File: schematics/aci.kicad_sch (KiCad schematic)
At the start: 10 parts, among them J1 From Tape, U11 LM339, U12 74HC10, U13 74HC02

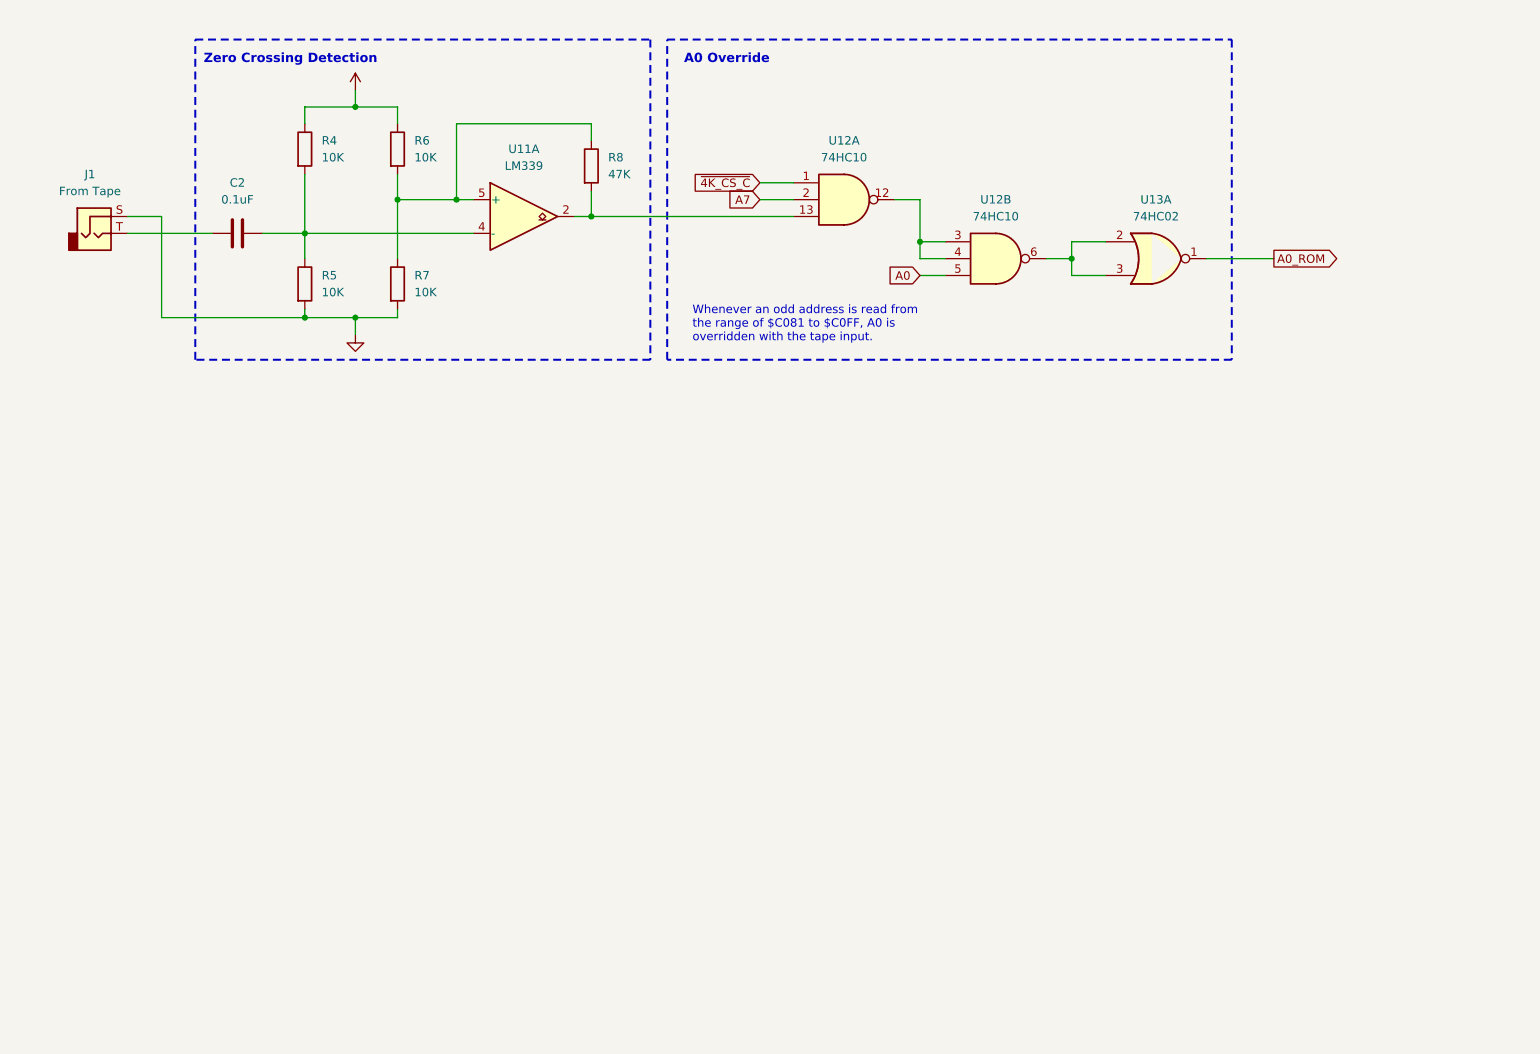
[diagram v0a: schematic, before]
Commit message: schematics updates
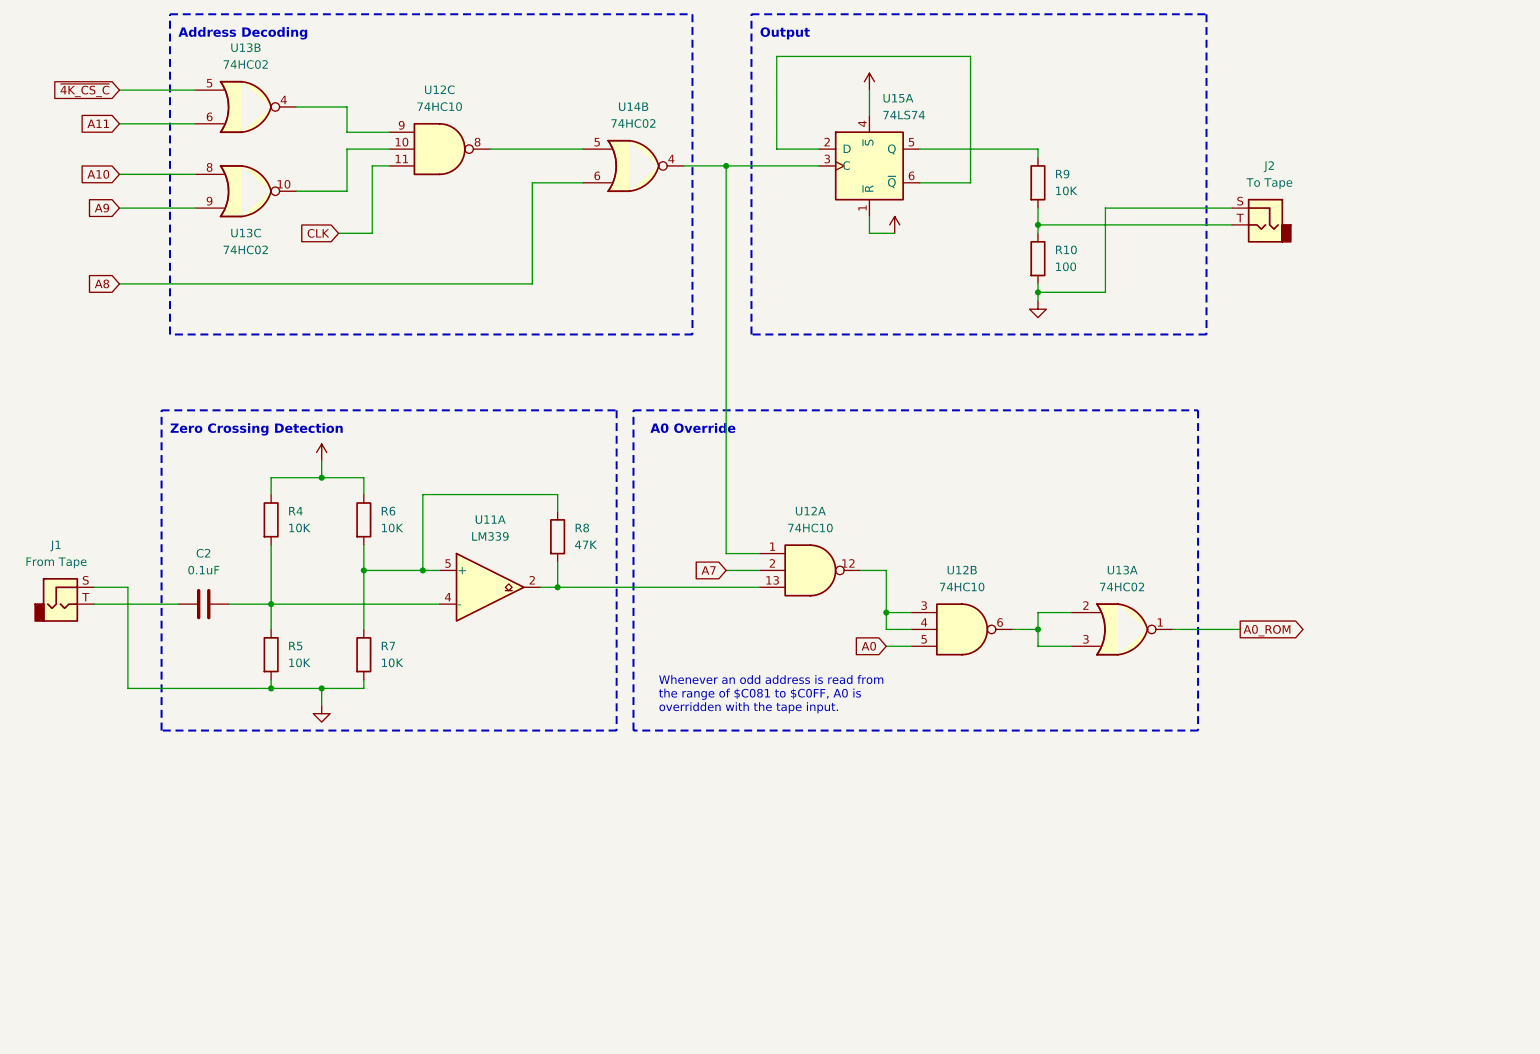
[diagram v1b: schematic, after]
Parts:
- added J2: To Tape, symbol Connector_Audio:AudioJack2
- added R10: 100, symbol Device:R
- added R9: 10K, symbol Device:R
- added unit 3 of U12
- added unit 3 of U13
- added unit 2 of U13
- added U14: 74HC02, symbol 74xx:74HC02
- added U15: 74LS74, symbol 74xx:74LS74
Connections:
- net GND: now also J2.S, R10.2
- net VCC: now also U15.1 (~{R}), U15.4 (~{S})
- net ~{4K_CS_C}: now also U13.5; no longer U12.1
- new net: J2.T, R10.1, R9.2
- new net: U12.10, U13.10
- new net: U12.8, U14.5
- new net: U12.9, U13.4
- new net: R9.1, U15.5 (Q)
- new net: U15.2 (D), U15.6 (~{Q})
- new net: U12.1, U14.4, U15.3 (C)
- new net A10: U13.8
- new net A11: U13.6
- new net A8: U14.6
- new net A9: U13.9
- new net CLK: U12.11
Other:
- note added: "Address Decoding"
- note added: "Output"
- moved on the sheet: C2, J1, R4, R5, R6, R7, R8, U11A, U12A, U12B, U13A

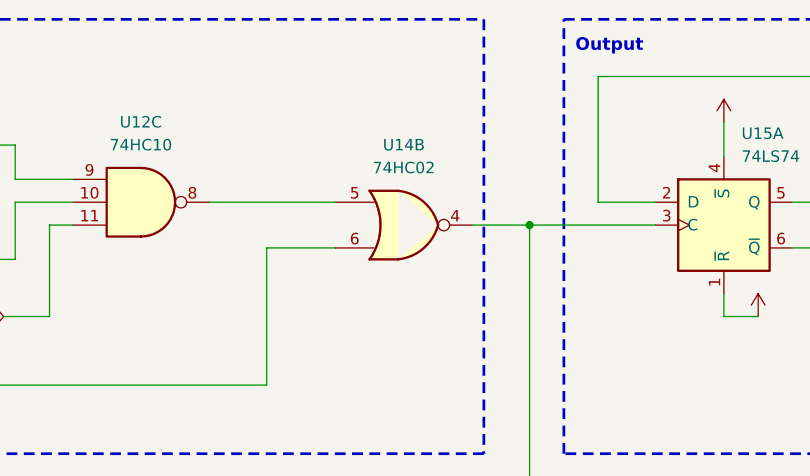
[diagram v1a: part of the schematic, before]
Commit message: minor correction to schematics
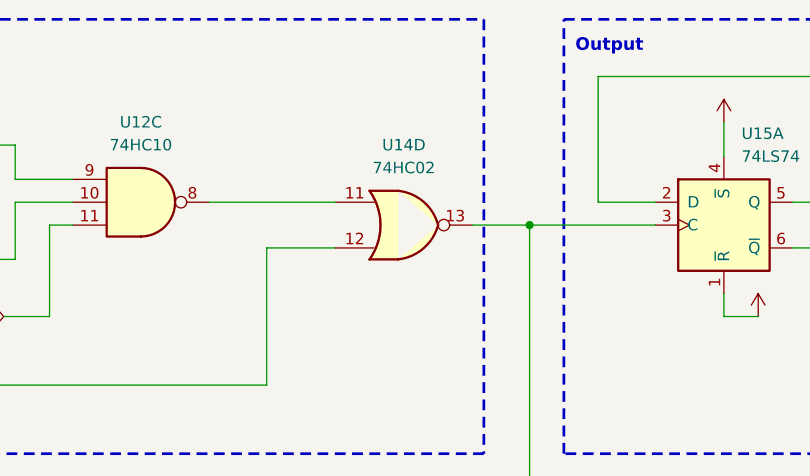
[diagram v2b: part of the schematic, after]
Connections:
- net A8: now also U14.12; no longer U14.6
- net at U12.8: now also U14.11; no longer U14.5
- net at U12.1, U15.3 (C): now also U14.13; no longer U14.4
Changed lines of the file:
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@@
     )
   )
-  (symbol (lib_id "74xx:74HC02") (at 127 44.45 0) (unit 2)
+  (symbol (lib_id "74xx:74HC02") (at 127 44.45 0) (unit 4)
     (in_bom yes) (on_board yes) (dnp no) (fields_autoplaced)
     (property "Reference" "U14" (at 127 35.56 0)
@@
       (project "apple-1"
         (path "/49da186c-18fb-4ced-8737-786ea50767d0/08d01d12-1e76-4903-ba4b-59c171f11e17"
-          (reference "U14") (unit 2)
+          (reference "U14") (unit 4)
         )
       )

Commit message: updates to schematics and 6502 source for ACI
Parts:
- R4, R5: value 10K -> 680K
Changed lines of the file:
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@@
       (effects (font (size 1.27 1.27)) (justify left))
     )
-    (property "Value" "10K" (at 74.93 99.06 0)
+    (property "Value" "680K" (at 74.93 99.06 0)
       (effects (font (size 1.27 1.27)) (justify left))
     )
@@
       (effects (font (size 1.27 1.27)) (justify left))
     )
-    (property "Value" "10K" (at 74.93 119.38 0)
-      (effects (font (size 1.27 1.27)) (justify left))
-    )
+    (property "Value" "680K" (at 74.93 119.38 0)
+      (effects (font (size 1.27 1.27)) (justify left))
+    )

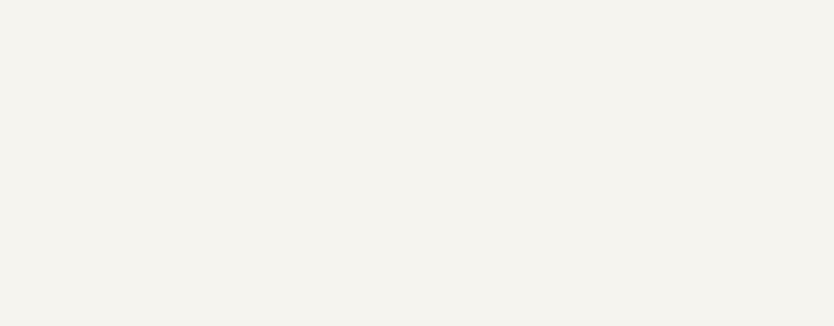
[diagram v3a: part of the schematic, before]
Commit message: added UART to design
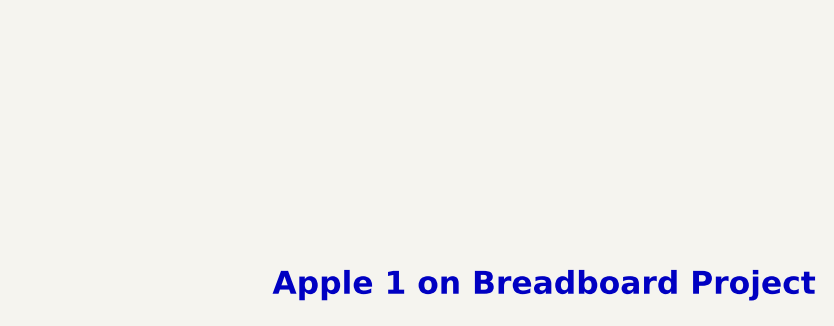
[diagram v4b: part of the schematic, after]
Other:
- note added: "Apple 1 on Breadboard Project"
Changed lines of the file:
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@@
     (effects (font (size 1.4 1.4) (thickness 0.28) bold) (justify left bottom))
+  )
+  (text "Apple 1 on Breadboard Project" (at 261.62 175.26 0)
+    (effects (font (size 2.54 2.54) (thickness 0.508) bold) (justify right bottom))
   )
   (text "Address Decoding" (at 58.42 25.4 0)
